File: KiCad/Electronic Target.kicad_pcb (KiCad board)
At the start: 2 copper layers, 43 parts, among them J1 Conn_02x06_Odd_Even, J2 Conn_02x04_Odd_Even, U1 LM339, U2 74HC74, U3 74HC74, U4 74HC00, U5 74LV8154, U6 74LV8154, U7 NMA0505SC, X1 8M0

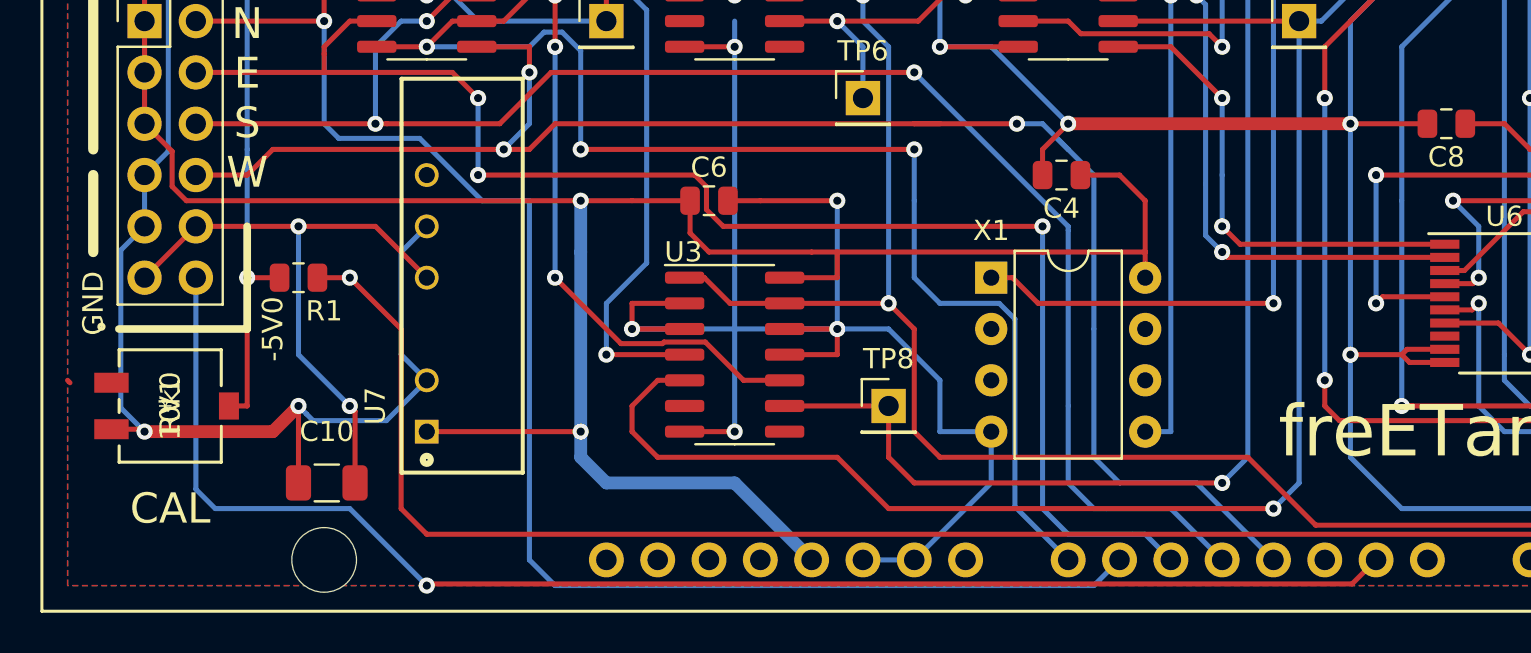
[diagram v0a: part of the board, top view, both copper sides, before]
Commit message: Corrections to PCB
Added load resistor to switching power supply
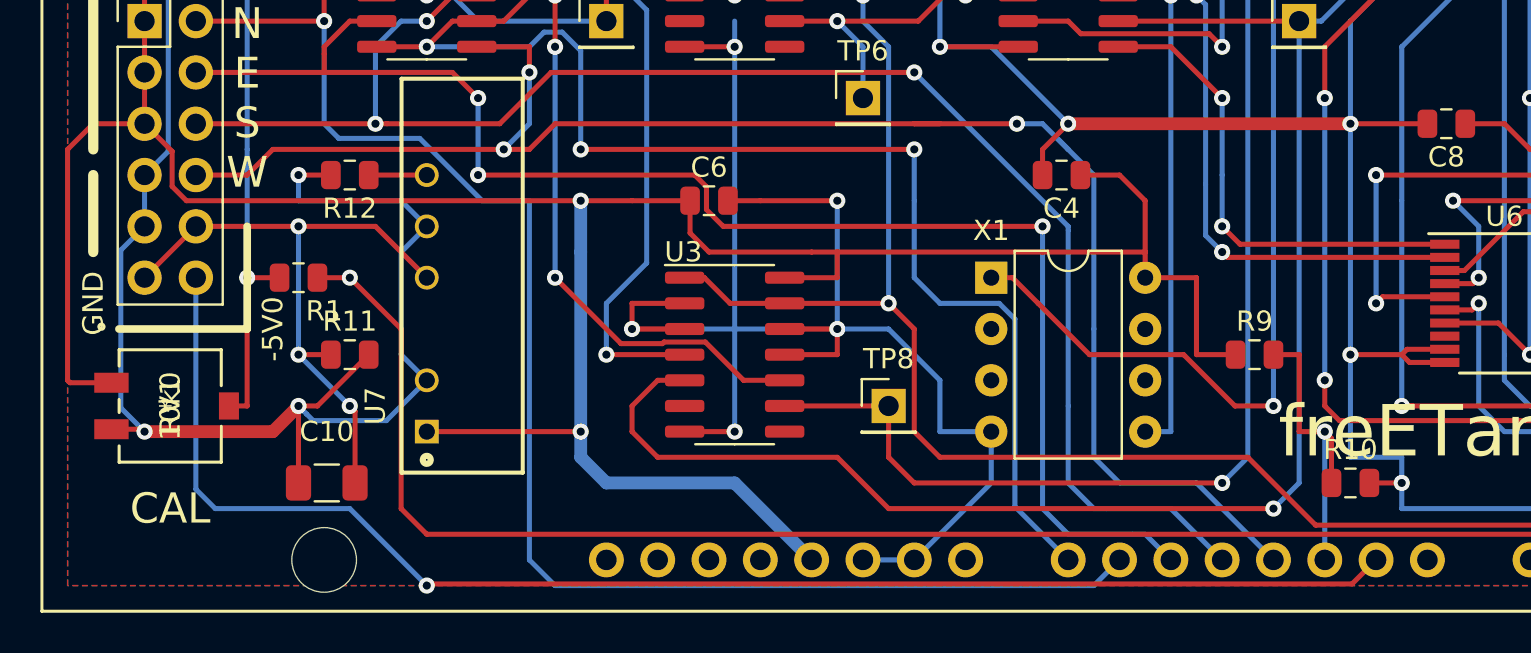
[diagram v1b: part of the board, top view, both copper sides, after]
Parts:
- added R10: 4K7, Resistor_SMD:R_0805_2012Metric, F.Cu at (181.6, 129.5)
- added R11: 10K0, Resistor_SMD:R_0805_2012Metric, F.Cu at (132.1, 123.2)
- added R12: 10K0, Resistor_SMD:R_0805_2012Metric, F.Cu at (132.1, 114.3)
- added R9: 4K7, Resistor_SMD:R_0805_2012Metric, F.Cu at (176.9, 123.2)
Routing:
- net VCC: track 346.5 -> 372.6 mm
- net GND: track 424.4 -> 441.8 mm, vias 23 -> 25
- net /BD_REV: track 0.00 -> 15.4 mm, vias 0 -> 1
- net /QUIET: track 73.1 -> 80.3 mm
- net Net-(R12-Pad1): track 0.00 -> 2.87 mm
- net Net-(C10-Pad1): track 29.9 -> 31.5 mm, vias 2 -> 3

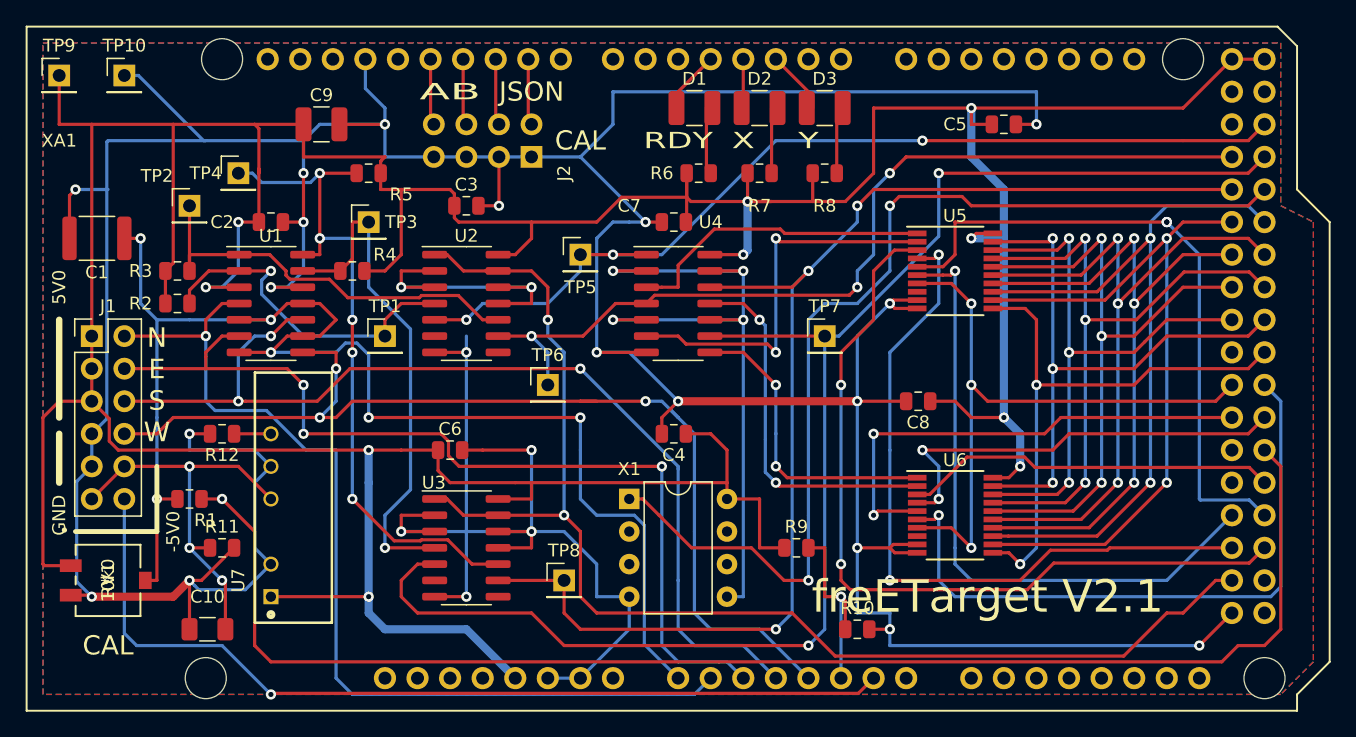
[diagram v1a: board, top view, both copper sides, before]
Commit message: Using digital thermometer
Changes to the circuit to support an I2C termometer in place of the RTD
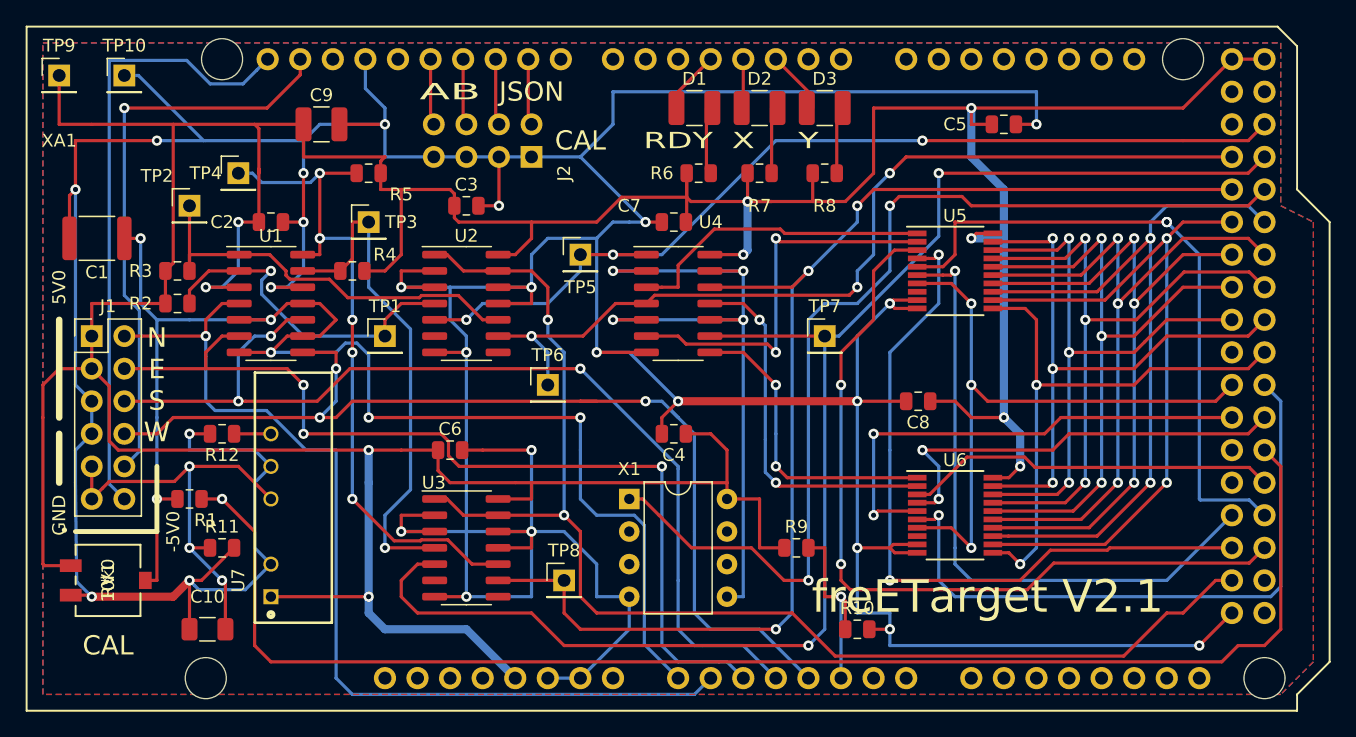
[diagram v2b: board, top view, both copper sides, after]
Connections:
- J1 pad 10: Net-(C10-Pad1) -> /SDA
- J1 pad 12: /TEMP -> /SCL
- J1 pad 5: VCC -> GND
- J1 pad 9: GND -> Net-(C10-Pad1)
- XA1 pad A6: /TEMP -> Net-(XA1-PadA6)
- XA1 pad SCL: Net-(XA1-PadSCL) -> /SCL
- XA1 pad SDA: Net-(XA1-PadSDA) -> /SDA
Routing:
- net /TEMP: track 71.3 -> 0.00 mm, vias 1 -> 0
- net /SCL: track 0.00 -> 48.6 mm
- net /SDA: track 0.00 -> 44.9 mm, vias 0 -> 1
- net GND: track 441.8 -> 464.3 mm, vias 25 -> 26
- net VCC: track 372.6 -> 366.9 mm
- net Net-(C10-Pad1): track 31.5 -> 34.1 mm

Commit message: Changed to I2C Temperature Sensor
The older RTD temperature sensor was replaced by an I2C one located on the main board.

This also brough in changes to the sensor module and additional data on the JSON shot info
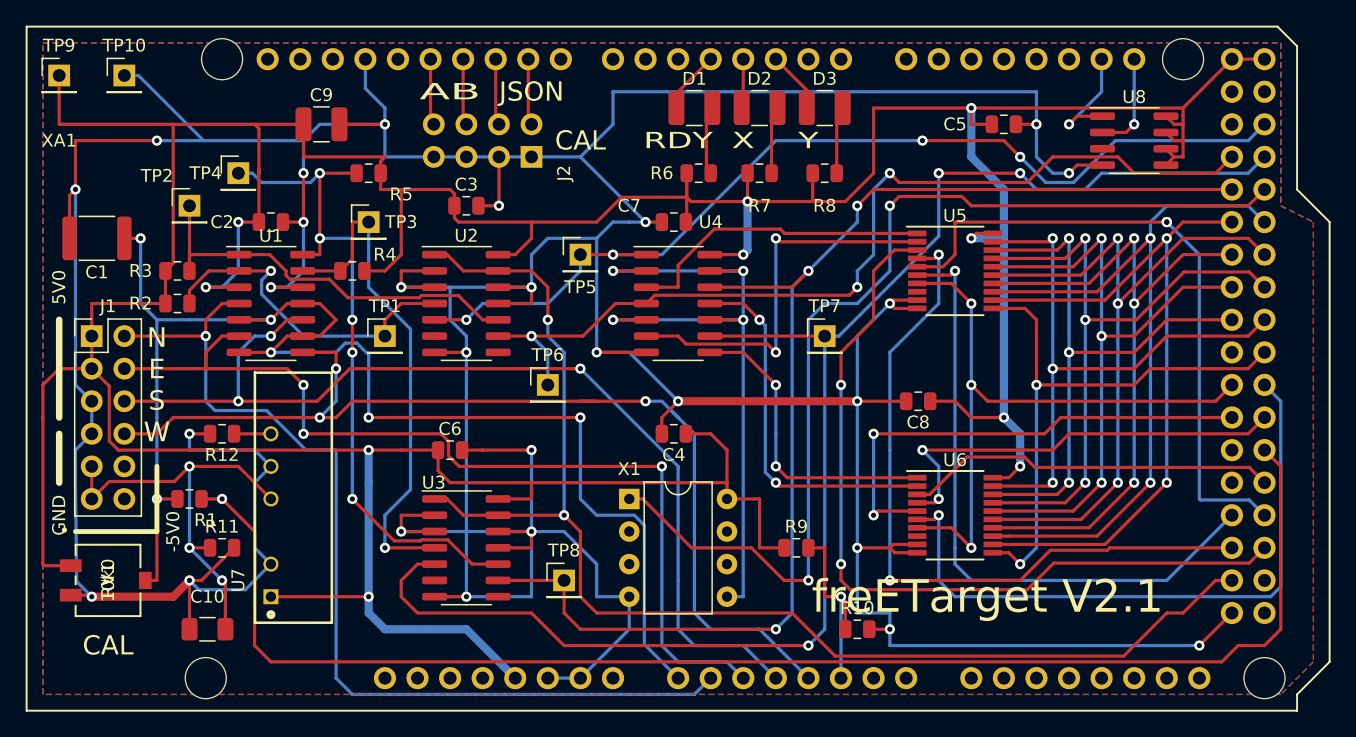
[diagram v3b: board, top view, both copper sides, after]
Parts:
- added U8: LM75AIMX_NOPB, Package_SO:SOIC-8_3.9x4.9mm_P1.27mm, F.Cu at (203.2, 91.4)
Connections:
- J1 pad 10: /SDA -> Net-(J1-Pad10)
- J1 pad 12: /SCL -> Net-(J1-Pad12)
- XA1 pad SCL: /SCL -> Net-(XA1-PadSCL)
- XA1 pad SDA: /SDA -> Net-(XA1-PadSDA)
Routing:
- net /SCL: track 48.6 -> 0.00 mm
- net /SDA: track 44.9 -> 0.00 mm, vias 1 -> 0
- net VCC: track 366.9 -> 376.4 mm
- net Net-(U8-Pad1): track 0.00 -> 9.00 mm, vias 0 -> 1
- net GND: track 464.3 -> 472.7 mm, vias 26 -> 27
- net Net-(U8-Pad2): track 0.00 -> 7.82 mm, vias 0 -> 1
- net /RUN_NORTH: track 74.4 -> 77.1 mm, vias 3 -> 4
- net /RUN_EAST: track 71.1 -> 72.7 mm
- net /RUN_SOUTH: track 114.3 -> 115.3 mm, vias 2 -> 3

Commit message: Adding DigiKey part numbers
Adding in DK part numbers for manufacturing
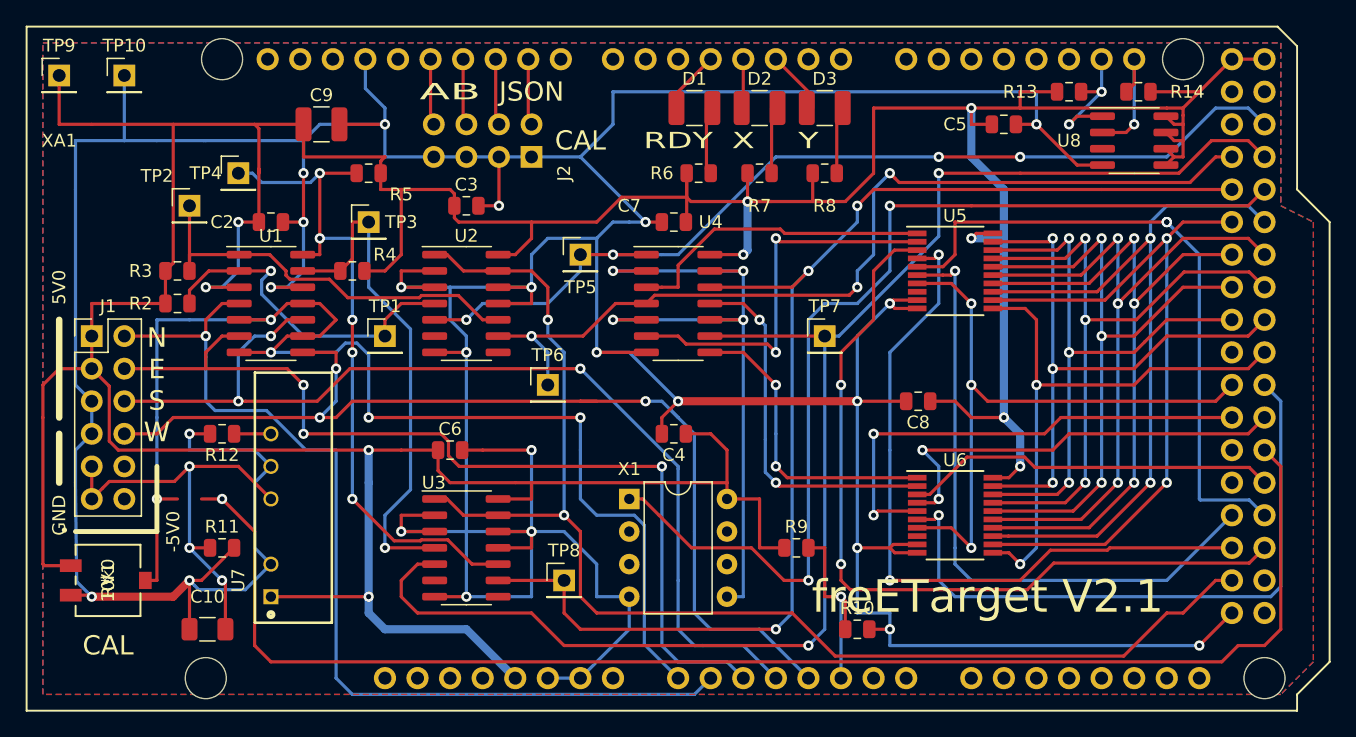
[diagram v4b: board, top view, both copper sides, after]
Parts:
- removed C1: CP, Resistor_SMD:R_1812_4532Metric
- removed R1: 4K7, Resistor_SMD:R_0805_2012Metric
- added R13: 4K7, Resistor_SMD:R_0805_2012Metric, F.Cu at (198.1, 87.6)
- added R14: 4K7, Resistor_SMD:R_0805_2012Metric, F.Cu at (203.5, 87.6)
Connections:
- XA1 pad D45: /VREF -> Net-(XA1-PadD45)
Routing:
- net Net-(XA1-PadD45): track 0.00 -> 110.2 mm, vias 0 -> 1
- net /VREF: track 110.2 -> 0.00 mm, vias 1 -> 0
- net GND: track 472.7 -> 463.5 mm, vias 27 -> 24
- net /V_FB: track 112.1 -> 104.0 mm, vias 6 -> 5
- net VCC: track 376.4 -> 384.4 mm
- net Net-(R14-Pad2): track 7.82 -> 11.1 mm
- net /RUN_NORTH: track 77.1 -> 75.4 mm
- net Net-(R13-Pad2): track 9.00 -> 10.6 mm, vias 1 -> 2
- net /RUN_EAST: track 72.7 -> 71.7 mm
- net /QUIET: track 80.3 -> 79.7 mm
- net /RUN_SOUTH: vias 3 -> 2
